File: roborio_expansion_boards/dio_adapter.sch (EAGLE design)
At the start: 20 parts

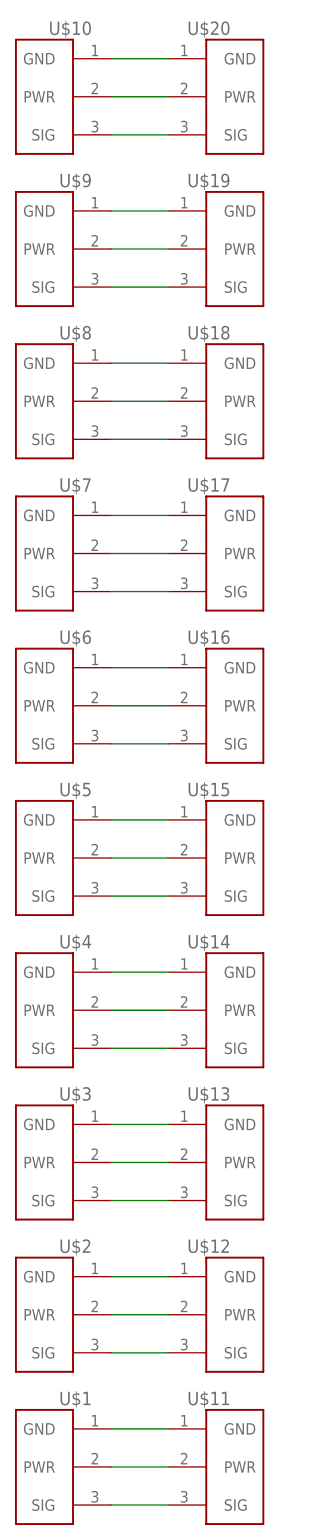
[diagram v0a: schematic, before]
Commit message: added capacitors to the power lines near each connector
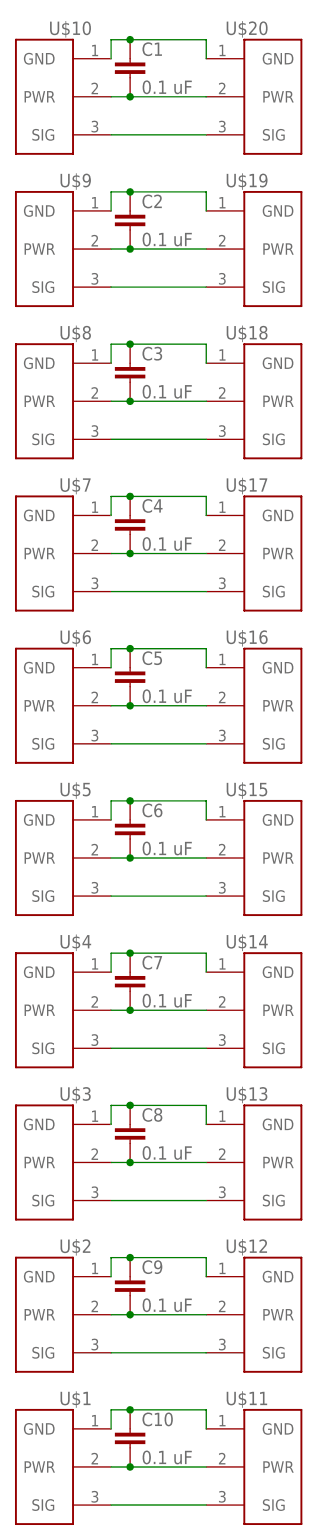
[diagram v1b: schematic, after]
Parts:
- added C1, C10, C2, C3, C4, C5, C6, C7, C8, C9: 0.1 uF, custom:CAP0603
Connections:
- net N$1: now also C1.1
- net N$10: now also C8.1, U$13.GND, U$3.GND; no longer U$17.GND, U$7.GND
- net N$11: now also C4.2
- net N$13: now also C7.1, U$14.GND, U$4.GND; no longer U$16.GND, U$6.GND
- net N$14: now also C5.2
- net N$16: now also C6.1
- net N$17: now also C6.2
- net N$19: now also C5.1, U$16.GND, U$6.GND; no longer U$14.GND, U$4.GND
- net N$2: now also C1.2
- net N$20: now also C7.2
- net N$22: now also C4.1, U$17.GND, U$7.GND; no longer U$13.GND, U$3.GND
- net N$23: now also C8.2
- net N$25: now also C3.1, U$18.GND, U$8.GND; no longer U$12.GND, U$2.GND
- net N$26: now also C9.2
- net N$28: now also C2.1, U$19.GND, U$9.GND; no longer U$1.GND, U$11.GND
- net N$29: now also C10.2
- net N$4: now also C10.1, U$1.GND, U$11.GND; no longer U$19.GND, U$9.GND
- net N$5: now also C2.2
- net N$7: now also C9.1, U$12.GND, U$2.GND; no longer U$18.GND, U$8.GND
- net N$8: now also C3.2
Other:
- moved on the sheet: U$11, U$12, U$13, U$14, U$15, U$16, U$17, U$18, U$19, U$20
